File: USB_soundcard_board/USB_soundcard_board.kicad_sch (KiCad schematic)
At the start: 111 parts, among them IC1 USBLC6-2SC6, IC2 CP2112-F03-GMR, IC3 CP2615-A02-GMR, IC4 USBLC6-2SC6, IC5 AP2112K-1.8, J1 TT04_BREAKOUT_REVB, U1 Raspberry Pi Pico

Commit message: Post-prototype tweaks in USB board schematic
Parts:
- C27, C34: value 3p -> 2p7
- C29, C30, L3: value DNP -> 0R
- L1: value 663n -> 650n; eshop (none) -> https://cz.mouser.com/ProductDetail/81-LQW18CNR65J0HD
- L2: value 191n -> 200n; eshop (none) -> https://cz.mouser.com/ProductDetail/81-LQW18ANR20G00D
- R35, R36, R5, R6: now not fitted
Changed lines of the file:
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@@
 		(in_bom yes)
 		(on_board yes)
-		(dnp no)
+		(dnp yes)
 		(property "Reference" "R5"
 			(at 369.57 34.29 0)
@@
 			)
 		)
-		(property "Value" "663n"
+		(property "Value" "650n"
 			(at 224.79 227.33 90)
 			(effects
@@
 			)
 		)
-		(property "eshop" ""
+		(property "eshop" "https://cz.mouser.com/ProductDetail/81-LQW18CNR65J0HD"
 			(at 224.79 229.87 0)
 			(effects
@@
 			)
 		)
-		(property "Value" "3p"
+		(property "Value" "2p7"
 			(at 220.98 256.5462 0)
 			(effects
@@
 		(at 129.54 71.12 0)
 		(unit 1)
-		(exclude_from_sim no)
+		(exclude_from_sim yes)
 		(in_bom yes)
 		(on_board yes)
@@
 			)
 		)
-		(property "Value" "DNP"
+		(property "Value" "0R"
 			(at 212.0963 204.47 90)
 			(effects
@@
 		(in_bom yes)
 		(on_board yes)
-		(dnp no)
+		(dnp yes)
 		(property "Reference" "R36"
 			(at 300.355 132.08 90)
@@
 			)
 		)
-		(property "Value" "3p"
+		(property "Value" "2p7"
 			(at 220.98 234.9562 0)
 			(effects
@@
 			)
 		)
-		(property "Value" "DNP"
+		(property "Value" "0R"
 			(at 237.4963 204.47 90)
 			(effects
@@
 		(in_bom yes)
 		(on_board yes)
-		(dnp no)
+		(dnp yes)
 		(property "Reference" "R35"
 			(at 300.355 129.54 90)
@@
 		(in_bom yes)
 		(on_board yes)
-		(dnp no)
+		(dnp yes)
 		(property "Reference" "R6"
 			(at 378.46 34.29 0)
@@
 			)
 		)
-		(property "Value" "DNP"
+		(property "Value" "0R"
 			(at 224.79 205.74 90)
 			(effects
@@
 			)
 		)
-		(property "Value" "191n"
+		(property "Value" "200n"
 			(at 232.41 234.9499 0)
 			(effects
@@
 			)
 		)
-		(property "eshop" ""
+		(property "eshop" "https://cz.mouser.com/ProductDetail/81-LQW18ANR20G00D"
 			(at 231.14 233.68 0)
 			(effects

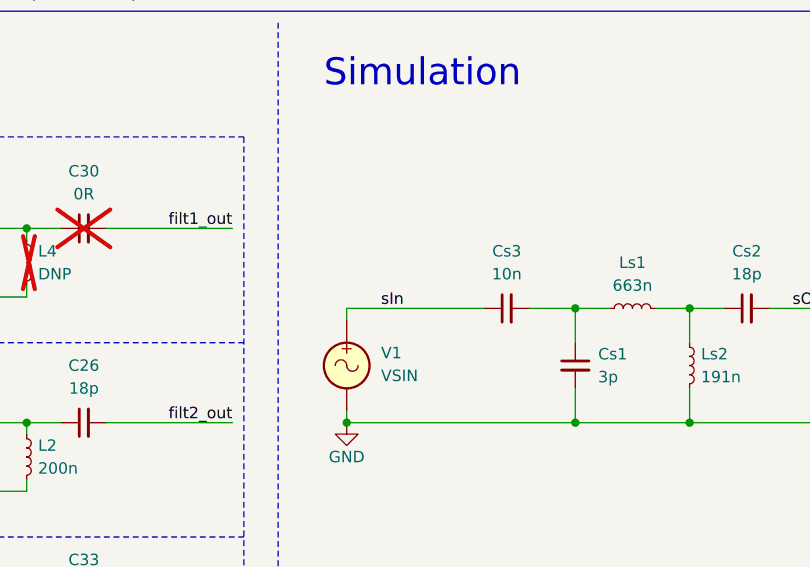
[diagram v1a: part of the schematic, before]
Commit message: Added filter input impedance trace to the simulation.
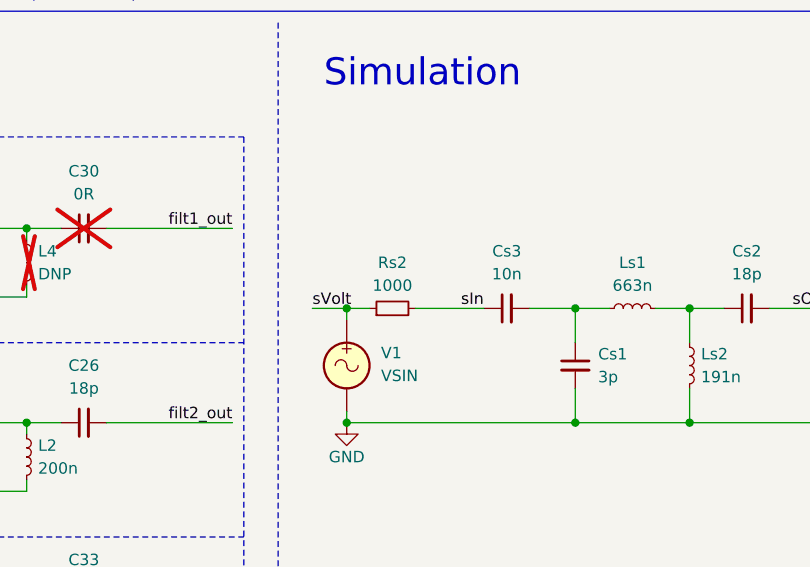
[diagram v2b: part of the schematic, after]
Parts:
- added Rs2: 1000, symbol Device:R_Small
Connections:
- net sIn: now also Rs2.2; no longer V1.1
- new net sVolt: Rs2.1, V1.1
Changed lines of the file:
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@@
 	)
 	(junction
+		(at 266.7 217.17)
+		(diameter 0)
+		(color 0 0 0 0)
+	)
+	(junction
 		(at 39.37 223.52)
 		(diameter 0)
@@
 	(wire
 		(pts
-			(xy 266.7 217.17) (xy 266.7 218.44)
-		)
-		(stroke
-			(width 0)
-			(type default)
-		)
-	)
-	(wire
-		(pts
 			(xy 127 118.11) (xy 127 133.35)
 		)
@@
 	(wire
 		(pts
+			(xy 262.89 217.17) (xy 266.7 217.17)
+		)
+		(stroke
+			(width 0)
+			(type default)
+		)
+	)
+	(wire
+		(pts
 			(xy 53.34 233.68) (xy 53.34 236.22)
 		)
@@
 	(wire
 		(pts
+			(xy 274.32 217.17) (xy 281.94 217.17)
+		)
+		(stroke
+			(width 0)
+			(type default)
+		)
+	)
+	(wire
+		(pts
 			(xy 170.18 20.32) (xy 170.18 21.59)
 		)
@@
 	(wire
 		(pts
-			(xy 266.7 217.17) (xy 281.94 217.17)
-		)
-		(stroke
-			(width 0)
-			(type default)
-		)
-	)
-	(wire
-		(pts
 			(xy 49.53 223.52) (xy 53.34 223.52)
 		)
@@
 	(wire
 		(pts
+			(xy 266.7 217.17) (xy 269.24 217.17)
+		)
+		(stroke
+			(width 0)
+			(type default)
+		)
+	)
+	(wire
+		(pts
 			(xy 262.89 58.42) (xy 265.43 58.42)
 		)
@@
 	(wire
 		(pts
+			(xy 266.7 217.17) (xy 266.7 218.44)
+		)
+		(stroke
+			(width 0)
+			(type default)
+		)
+	)
+	(wire
+		(pts
 			(xy 199.39 55.88) (xy 217.17 55.88)
 		)
@@
 		)
 	)
+	(label "sVolt"
+		(at 262.89 217.17 0)
+		(fields_autoplaced yes)
+		(effects
+			(font
+				(size 1.27 1.27)
+			)
+			(justify left bottom)
+		)
+	)
 	(label "i2c_sda"
 		(at 224.79 43.18 180)
@@
 	)
 	(label "sIn"
-		(at 270.51 217.17 0)
+		(at 279.4 217.17 0)
 		(fields_autoplaced yes)
 		(effects
@@
 					(unit 1)
 				)
+			)
+		)
+	)
+	(symbol
+		(lib_id "Device:R_Small")
+		(at 271.78 217.17 90)
+		(unit 1)
+		(exclude_from_sim no)
+		(in_bom no)
+		(on_board no)
+		(dnp no)
+		(fields_autoplaced yes)
+		(property "Reference" "Rs2"
+			(at 271.78 212.09 90)
+			(effects
+				(font
+					(size 1.27 1.27)
+				)
+			)
+		)
+		(property "Value" "1000"
+			(at 271.78 214.63 90)
+			(effects
+				(font
+					(size 1.27 1.27)
+				)
+			)
+		)
+		(property "Footprint" ""
+			(at 271.78 217.17 0)
+			(effects
+				(font
+					(size 1.27 1.27)
+				)
+				(hide yes)
+			)
+		)
+		(property "Datasheet" "~"
+			(at 271.78 217.17 0)
+			(effects
+				(font
+					(size 1.27 1.27)
+				)
+				(hide yes)
+			)
+		)
+		(property "Description" "Resistor, small symbol"
+			(at 271.78 217.17 0)
+			(effects
+				(font
+					(size 1.27 1.27)
+				)
+				(hide yes)
+			)
+		)
+		(property "eshop" ""
+			(at 271.78 217.17 0)
+			(effects
+				(font
+					(size 1.27 1.27)
+				)
+				(hide yes)
+			)
+		)
+		(pin "2"
+		)
+		(pin "1"
+		)
+		(instances
+			(project "USB_soundcard_board"
+				(path "/167953b6-a2da-4a48-9cbd-ef5a63adcb68"
+					(reference "Rs2")
+					(unit 1)
+				)
